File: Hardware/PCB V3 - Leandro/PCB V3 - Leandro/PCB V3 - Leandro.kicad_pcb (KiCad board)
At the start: 2 copper layers, 80 x 35 mm, 15 parts, among them J1 Bateria (-), J10 MOTOR_DER, J2 Bateria (+), J3 Sensor TATAMI FD, J4 SWITCH, J5 Sensor TATAMI FI, J6 STEP_DOWN, J7 IR_FD, J8 IR_FI, J9 MOTOR_IZQ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

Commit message: termine la placa hay que ver que dice bustos
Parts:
- J1: value Bateria (-) -> Bateria (+)
- J2: value Bateria (+) -> Bateria (-)
- moved Display1 174.6 mm to (89.5, 101.5), turned to -90 degrees
- moved J6 36.7 mm to (153.5, 91.0)
- moved J5 19.9 mm to (100.0, 83.5)
- moved J8 17.0 mm to (100.0, 89.5)
- moved J3 11.2 mm to (100.0, 86.5)
- moved BZ1 10.0 mm to (157.0, 108.0), turned to 0 degrees
- moved J7 8.50 mm to (100.0, 92.5)
- moved J4 6.80 mm to (161.0, 85.5)
- moved J2 6.00 mm to (166.0, 105.0)
- moved J1 5.25 mm to (166.0, 94.2)
- moved J9 5.00 mm to (139.0, 101.0), turned to 180 degrees
- moved J10 4.50 mm to (150.0, 100.5)
- moved SW1 2.00 mm to (145.7, 88.5)
- moved SW2 2.00 mm to (141.7, 88.5)
- moved U1 1.00 mm to (136.0, 96.0)
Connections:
- SW1 pad 1: GND -> +5V
- SW2 pad 1: GND -> +5V
- U1 pad 24: /M1A -> /M2A
- U1 pad 26: /M2A -> /M1A
- U1 pad 29: /BUZZER -> /M1B
- U1 pad 3: /START -> unconnected-(U1-Pad3)
- U1 pad 30: /M1B -> /BUZZER
- U1 pad 4: /ESTRATEGIA -> /START
- U1 pad 5: /IR_D -> /ESTRATEGIA
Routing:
- net +5V: track 0.00 -> 108.3 mm
- net /IR_FD: track 0.00 -> 45.0 mm
- net /IR_FI: track 0.00 -> 41.1 mm
- net /SCL: track 0.00 -> 38.0 mm
- net /TATAMI_FD: track 0.00 -> 34.1 mm
- net /SDA: track 0.00 -> 34.0 mm
- net /TATAMI_FI: track 0.00 -> 29.3 mm
- net GND: track 0.00 -> 27.8 mm, vias 0 -> 3
- net /Vstep: track 0.00 -> 14.1 mm
- net /M1A: track 0.00 -> 10.3 mm
- net /VBAT: track 0.00 -> 10.1 mm
- net /M1B: track 0.00 -> 9.26 mm
- net /M2B: track 0.00 -> 8.42 mm
- net /M2A: track 0.00 -> 8.04 mm
- net /START: track 0.00 -> 4.70 mm
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- added copper zone on B.Cu, net GND
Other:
- board size 80 x 35 mm -> 80 x 30 mm
- board text added: "Sami v3"

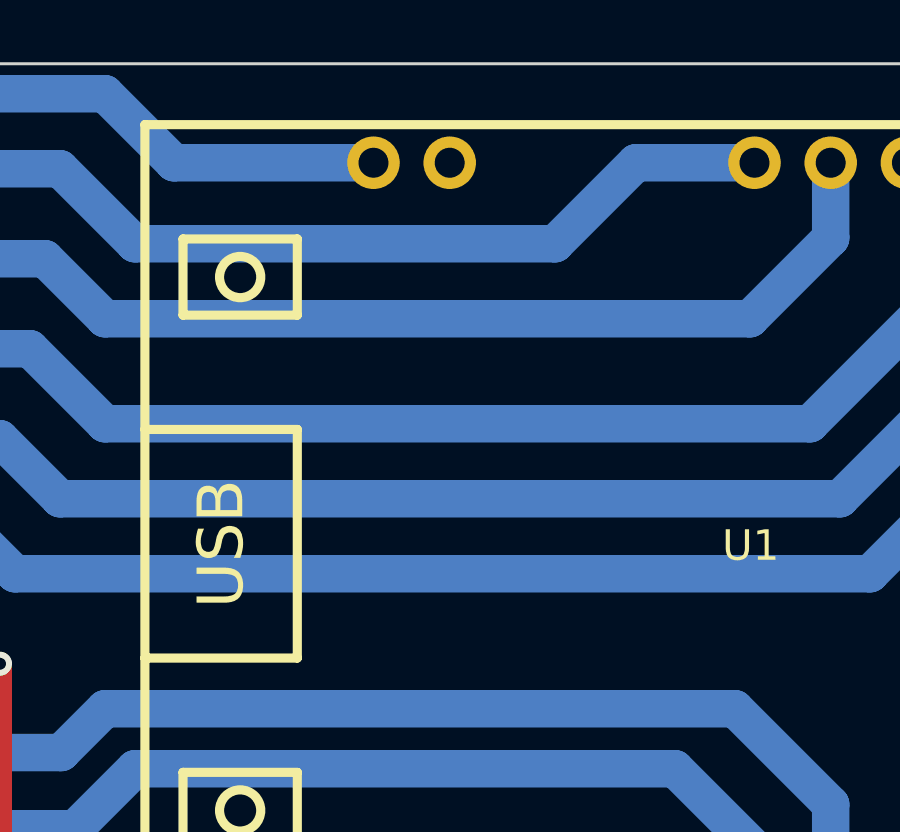
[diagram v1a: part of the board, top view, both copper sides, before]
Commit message: corregi algo quevi de gnd
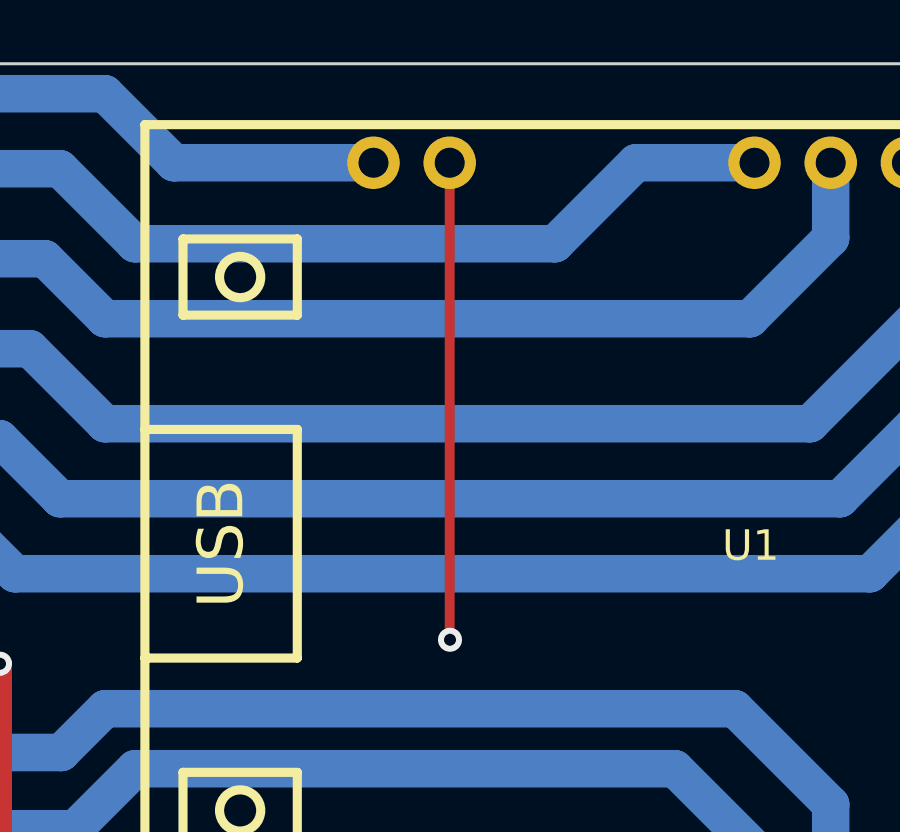
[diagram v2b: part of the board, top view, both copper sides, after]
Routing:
- net GND: track 27.8 -> 43.7 mm, vias 3 -> 4
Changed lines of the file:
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@@
   (segment (start 154.5 108) (end 155.73 108) (width 1) (layer "B.Cu") (net 1))
   (segment (start 152.51 108.7) (end 153.8 108.7) (width 1) (layer "B.Cu") (net 1))
+  (segment (start 119.49 99.19) (end 119.49 83.3) (width 0.33) (layer "F.Cu") (net 2))
+  (segment (start 119.5 99.2) (end 119.49 99.19) (width 0.33) (layer "F.Cu") (net 2))
   (segment (start 104.5 100) (end 104.5 108) (width 0.8) (layer "F.Cu") (net 2))
   (via (at 104.5 100) (size 0.8) (drill 0.4) (layers "F.Cu" "B.Cu") (free) (net 2))
   (via (at 104.5 108) (size 0.8) (drill 0.4) (layers "F.Cu" "B.Cu") (free) (net 2))
+  (via (at 119.5 99.2) (size 0.8) (drill 0.4) (layers "F.Cu" "B.Cu") (net 2))
   (via (at 159.5 91) (size 2) (drill 1) (layers "F.Cu" "B.Cu") (free) (net 2))
   (segment (start 158.73 107.54) (end 158.27 108) (width 1.5) (layer "B.Cu") (net 2))

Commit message: falta la correccion de Bustos y diseñar el svg
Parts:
- removed J2: Bateria (-), EESTN5:BORNERA2_AZUL
- removed J4: SWITCH, EESTN5:SW_SPDT_TH_Vertical
- moved Display1 16.1 mm to (95.2, 116.5), turned to 0 degrees
- moved J1 10.5 mm to (156.5, 98.8)
- moved J6 4.67 mm to (149.0, 89.8), turned to 90 degrees
- moved J10 4.51 mm to (146.2, 103.0)
- moved J9 3.20 mm to (136.5, 103.0)
- moved J3 2.26 mm to (100.2, 88.8)
- moved J5 2.26 mm to (100.2, 85.8)
- moved J7 2.26 mm to (100.2, 94.8)
- moved J8 2.26 mm to (100.2, 91.8)
- moved SW1 0.68 mm to (145.0, 88.5)
- moved SW2 0.32 mm to (142.0, 88.5)
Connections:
- J1 pad 1: /VBAT -> GND
- J1 pad 2: /VBAT -> /Vstep
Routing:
- net GND: track 43.7 -> 3.75 mm, vias 4 -> 1
- net /VBAT: track 10.1 -> 0.00 mm
- net +5V: track 108.3 -> 100.7 mm
- net /SCL: track 38.0 -> 43.2 mm
- net /M1A: track 10.3 -> 6.26 mm
- net /Vstep: track 14.1 -> 10.4 mm
- net /M1B: track 9.26 -> 6.22 mm
- net /M2B: track 8.42 -> 6.10 mm
- net /IR_FI: track 41.1 -> 39.3 mm
- net /TATAMI_FI: track 29.3 -> 27.9 mm
- net /IR_FD: track 45.0 -> 43.7 mm
- net /TATAMI_FD: track 34.1 -> 33.1 mm
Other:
- board size 80 x 30 mm -> 70.2 x 30 mm

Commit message: placa para fabricar ya
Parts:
- added H1: Mounting_Hole, EESTN5:pad_3mm, F.Cu at (174.2, 80.3)
- added H2: Mounting_Hole, EESTN5:pad_3mm, F.Cu at (161.7, 87.8)
- added J2: IR_COSTADO, EESTN5:Pin_Strip_3, F.Cu at (117.0, 90.9)
- moved J1 22.7 mm to (178.0, 91.5)
- moved BZ1 21.6 mm to (177.2, 100.5)
- moved Display1 18.2 mm to (112.0, 109.3)
- moved J6 18.2 mm to (165.7, 82.5)
- moved J3 18.1 mm to (117.0, 81.8)
- moved J5 18.1 mm to (117.0, 78.8)
- moved J7 18.1 mm to (117.0, 87.8)
- moved J8 18.1 mm to (117.0, 84.8)
- moved J9 17.5 mm to (152.5, 95.8)
- moved J10 16.6 mm to (161.2, 95.8)
- moved SW1 16.2 mm to (159.5, 81.3)
- moved SW2 15.3 mm to (155.5, 81.3)
- moved U1 15.1 mm to (149.1, 88.5)
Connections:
- U1 pad 6: /IR_FD -> /IR_COSTADO
- U1 pad 7: /IR_FI -> /IR_FD
- U1 pad 8: /IR_I -> /IR_FI
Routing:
- net /IR_COSTADO: track 0.00 -> 43.6 mm
- net /BUZZER: track 3.51 -> 10.6 mm
- net /IR_FD: track 43.7 -> 38.7 mm
- net /IR_FI: track 39.3 -> 34.5 mm
- net /Vstep: track 10.4 -> 15.2 mm
- net /SDA: track 34.4 -> 30.0 mm
- net /SCL: track 43.2 -> 39.2 mm
- net /TATAMI_FD: track 33.1 -> 29.4 mm
- net /TATAMI_FI: track 27.9 -> 24.5 mm
- net GND: track 3.75 -> 0.73 mm, vias 1 -> 0
- net /M2A: track 7.66 -> 5.58 mm
- net /M1A: track 6.26 -> 7.62 mm
- net /START: track 4.42 -> 5.56 mm
- net +5V: track 100.7 -> 99.7 mm
- net /M2B: track 6.10 -> 7.00 mm
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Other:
- board size 70.2 x 30 mm -> 75.2 x 32 mm
